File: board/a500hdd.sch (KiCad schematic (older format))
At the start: 35 parts, among them J1 Conn_01x04_Male, U1 ata_connector, U2 ata_connector44, U3 74LS04, U4 a500exp, U5 74LS00, U6 74LS08, U7 74LS08, U8 a500exp, U9 a500exp

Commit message: fixed activity LED on schematic?
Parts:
- removed unit 1 of U5
- added R19, R20: 10k, Capacitor_SMD:C_0805_2012Metric, symbol Device:R
- added unit 6 of U3
- added unit 4 of U5
- R18: value 4k7 -> 10k
- U3: value 74LS04 -> 74HCT14; symbol 74xx:74LS04 -> 74xx:74LS14
- U5: value 74LS00 -> 74HCT00
- U6, U7: value 74LS08 -> 74HCT08
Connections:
- net labels added: ~ATA40_ACTILED, ~ATA44_ACTILED
- net labels removed: B11, B9, ~ATA_ACTILED
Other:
- moved on the sheet: C1, C2, C3, C4, D1, R17, U5E

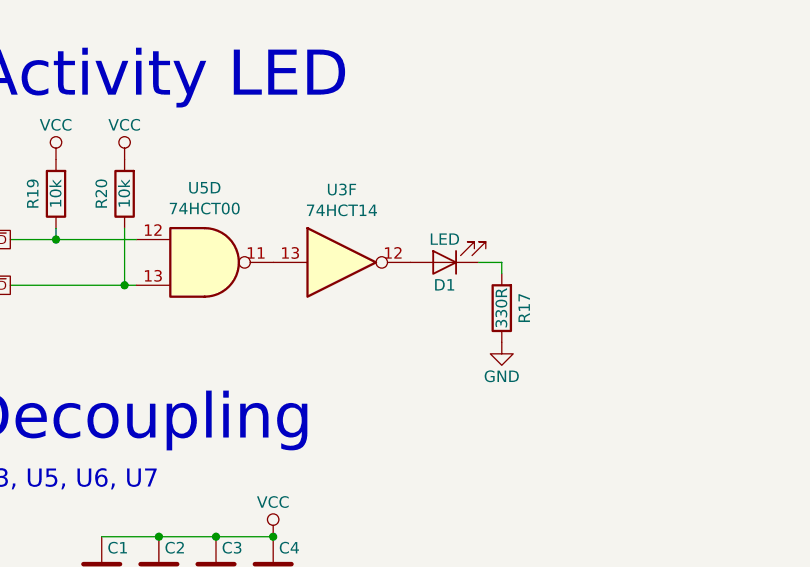
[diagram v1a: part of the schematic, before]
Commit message: Single negation of LED signal by NAND should be enough
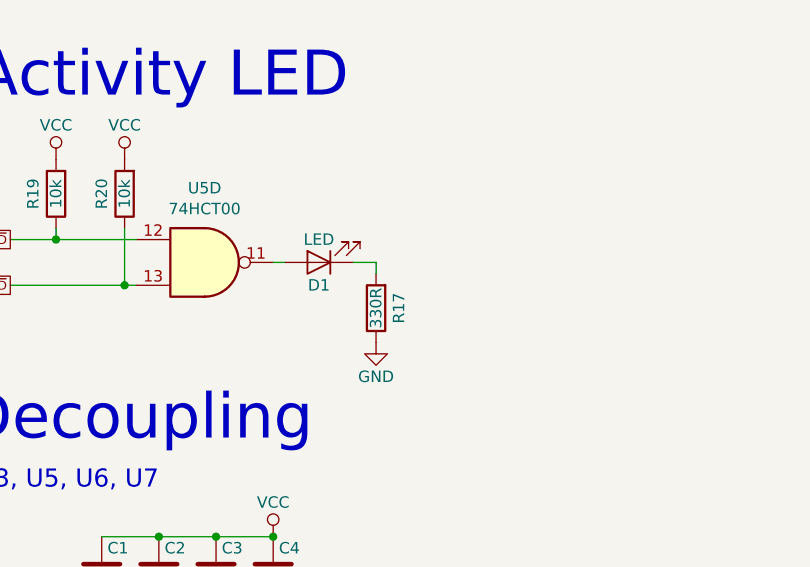
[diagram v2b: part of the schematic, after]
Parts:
- removed unit 6 of U3
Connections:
- wire segments 240 -> 241
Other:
- moved on the sheet: D1, R17
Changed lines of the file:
@@
 L Device:R R17
 U 1 1 59849A7F
-P 7900 5800
-F 0 "R17" V 7800 5800 50  0000 C CNN
-F 1 "330R" V 7900 5800 50  0000 C CNN
-F 2 "Capacitor_SMD:C_0805_2012Metric" V 7830 5800 50  0001 C CNN
-F 3 "" H 7900 5800 50  0000 C CNN
-	1    7900 5800
+P 7350 5800
+F 0 "R17" V 7250 5800 50  0000 C CNN
+F 1 "330R" V 7350 5800 50  0000 C CNN
+F 2 "Capacitor_SMD:C_0805_2012Metric" V 7280 5800 50  0001 C CNN
+F 3 "" H 7350 5800 50  0000 C CNN
+	1    7350 5800
 	-1   0    0    1
 $EndComp
@@
 L Device:LED D1
 U 1 1 59849BB3
-P 7650 5600
-F 0 "D1" H 7650 5700 50  0000 C CNN
-F 1 "LED" H 7650 5500 50  0000 C CNN
-F 2 "LED_SMD:LED_0805_2012Metric" H 7650 5600 50  0001 C CNN
-F 3 "" H 7650 5600 50  0000 C CNN
-	1    7650 5600
+P 7100 5600
+F 0 "D1" H 7100 5700 50  0000 C CNN
+F 1 "LED" H 7100 5500 50  0000 C CNN
+F 2 "LED_SMD:LED_0805_2012Metric" H 7100 5600 50  0001 C CNN
+F 3 "" H 7100 5600 50  0000 C CNN
+	1    7100 5600
 	-1   0    0    1
 $EndComp
 Wire Wire Line
-	7900 5600 7900 5650
+	7350 5600 7350 5650
 $Comp
 L power:GND #PWR09
 U 1 1 59849E9B
-P 7900 5950
-F 0 "#PWR09" H 7900 5700 50  0001 C CNN
-F 1 "GND" H 7900 5800 50  0000 C CNN
-F 2 "" H 7900 5950 50  0000 C CNN
-F 3 "" H 7900 5950 50  0000 C CNN
-	1    7900 5950
+P 7350 5950
+F 0 "#PWR09" H 7350 5700 50  0001 C CNN
+F 1 "GND" H 7350 5800 50  0000 C CNN
+F 2 "" H 7350 5950 50  0000 C CNN
+F 3 "" H 7350 5950 50  0000 C CNN
+	1    7350 5950
 	1    0    0    -1
 $EndComp
@@
 	950  3400 1050 3400
 Wire Wire Line
-	7800 5600 7900 5600
+	7250 5600 7350 5600
 Wire Wire Line
 	1450 10700 1550 10700
@@
 	1    0    0    -1
 $EndComp
-$Comp
-L 74xx:74LS14 U3
-U 6 1 5BB5917B
-P 7200 5600
-F 0 "U3" H 7200 5917 50  0000 C CNN
-F 1 "74HCT14" H 7200 5826 50  0000 C CNN
-F 2 "Package_SO:SOIC-14_3.9x8.7mm_P1.27mm" H 7200 5600 50  0001 C CNN
-F 3 "http://www.ti.com/lit/gpn/sn74LS04" H 7200 5600 50  0001 C CNN
-	6    7200 5600
-	1    0    0    -1
-$EndComp
 Wire Wire Line
 	5950 5500 6300 5500
+Wire Wire Line
+	6900 5600 6950 5600
 Wire Bus Line
 	5000 1450 5000 3100

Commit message: added clockport connectors
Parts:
- removed C1: 0.1uF, Capacitor_SMD:C_0805_2012Metric, symbol Device:C
- removed JP1, JP2: SolderJumper_2_Bridged, Jumper:SolderJumper-2_P1.3mm_Open_Pad1.0x1.5mm, symbol Jumper:SolderJumper_2_Bridged
- removed U3: 74HCT14, Package_SO:SOIC-14_3.9x8.7mm_P1.27mm, symbol 74xx:74LS14
- removed unit 2 of U5
- removed unit 3 of U5
- removed U6, U7: 74HCT08, Package_SO:SOIC-14_3.9x8.7mm_P1.27mm, symbol 74xx:74LS08
- added C3, C5, C6, C7, C8: 0.1uF, Capacitor_SMD:C_0805_2012Metric, symbol Device:C
- added D1, D3: LED, LED_SMD:LED_0805_2012Metric, symbol Device:LED
- added J1: Conn_02x03_Odd_Even, symbol Connector_Generic:Conn_02x03_Odd_Even
- added JP1: Jumper_NO_Small, symbol Jumper:SolderJumper_2_Open
- added JP2, JP3, JP4, JP5: SolderJumper_3_Open, symbol Jumper:SolderJumper_3_Open
- added R17, R18, R19: 10k, Capacitor_SMD:C_0805_2012Metric, symbol Device:R
- added R20, R23: 330R, Capacitor_SMD:C_0805_2012Metric, symbol Device:R
- added U1, U7: 74LS688, symbol 74xx:74LS688
- added U10, U12: clockport_connector, symbol a500hdd:clockport_connector
- added unit 1 of U3
- added unit 3 of U3
- added unit 4 of U3
- added U4: 74LS139, symbol 74xx:74LS139
- added U5, U6, U8, U9: 74HC245, symbol 74xx:74HC245
- renumbered C2 to C1, C3 to C2, D1 to D2, J1 to J2, R19 to R21, R20 to R22, R17 to R24, R18 to R25, U1 to U11, U2 to U13, U8 to U14, U9 to U15, U4 to U2, U5 to U3
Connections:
- net labels added: A12, A13, A14, A15, A2, A3, A4, A5, ADDR, ATA_ACTI, ATA_EN, CP_ACTI, CP_CS0, CP_CS1, CP_CS2, CP_CS3, CP_EN, INT6, UADDR, UDATA, ~ATA_CS2, ~ATA_CS3, ~CP_CSA, ~CP_CSB, ~IOR, ~IOW, ~RESET
- net labels removed: ATA_A0, ATA_A1, ATA_A2, ENABLE, ~ATA_RD, ~ATA_RESET, ~ATA_WR
- wire segments 241 -> 468
- no-connect marks 54 -> 53
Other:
- note added: "Address buffering"
- note added: "Buffers"
- note added: "Clockport Enable"
- note added: "Clockport connectors"
- note added: "Data buffering"
- note added: "Decoders"
- note added: "Decoupling & power"
- note added: "IDE40 Power"
- note added: "IO Read/Write"
- note added: "LEDs"
- note added: "Unused"
- note added: "~CS~ demux"
- note added: "~CS~ selection"
- note removed: "(optional)"
- note removed: "ATA Read/Write"
- note removed: "Activity LED"
- note removed: "Decoupling"
- note removed: "IDE Power"
- note removed: "U3, U5, U6, U7"
- note removed: "~CS~ swap"
- moved on the sheet: C1, C2, D2, J2, R1, R10, R11, R12, R13, R14, R15, R16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

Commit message: assignments done
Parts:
- J1: footprint (none) -> Connector_PinHeader_2.54mm:PinHeader_2x03_P2.54mm_Vertical
- JP1: footprint (none) -> Connector_PinHeader_2.54mm:PinHeader_1x02_P2.54mm_Vertical
- JP2, JP3, JP4, JP5: footprint (none) -> Connector_PinHeader_2.54mm:PinHeader_1x03_P2.54mm_Vertical
- U1, U5, U6, U7, U8, U9: footprint (none) -> Package_SO:TSSOP-20_4.4x6.5mm_P0.65mm
- U10, U12: footprint (none) -> Connector_PinHeader_2.00mm:PinHeader_2x11_P2.00mm_Vertical
- U3: footprint Package_SO:SOIC-14_3.9x8.7mm_P1.27mm -> Package_SO:TSSOP-14_4.4x5mm_P0.65mm
- U4: footprint (none) -> Package_SO:TSSOP-16_4.4x5mm_P0.65mm
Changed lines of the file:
@@
 F 0 "U3" H 2450 7200 50  0000 L CNN
 F 1 "74HCT00" H 2550 6850 50  0000 L CNN
-F 2 "Package_SO:SOIC-14_3.9x8.7mm_P1.27mm" H 2700 6850 50  0001 C CNN
+F 2 "Package_SO:TSSOP-14_4.4x5mm_P0.65mm" H 2700 6850 50  0001 C CNN
 F 3 "http://www.ti.com/lit/gpn/sn74ls00" H 2700 6850 50  0001 C CNN
 	5    2700 6850
@@
 F 0 "U3" H 6800 9475 50  0000 C CNN
 F 1 "74HCT00" H 6800 9384 50  0000 C CNN
-F 2 "Package_SO:SOIC-14_3.9x8.7mm_P1.27mm" H 6800 9150 50  0001 C CNN
+F 2 "Package_SO:TSSOP-14_4.4x5mm_P0.65mm" H 6800 9150 50  0001 C CNN
 F 3 "http://www.ti.com/lit/gpn/sn74ls00" H 6800 9150 50  0001 C CNN
 	2    6800 9150
@@
 F 0 "U1" H 1250 10750 50  0000 L CNN
 F 1 "74LS688" H 1650 8600 50  0000 L CNN
-F 2 "" H 1550 9700 50  0001 C CNN
+F 2 "Package_SO:TSSOP-20_4.4x6.5mm_P0.65mm" H 1550 9700 50  0001 C CNN
 F 3 "http://www.ti.com/lit/gpn/sn74LS688" H 1550 9700 50  0001 C CNN
 	1    1550 9700
@@
 F 0 "U7" H 3700 10750 50  0000 L CNN
 F 1 "74LS688" H 4100 8600 50  0000 L CNN
-F 2 "" H 4000 9700 50  0001 C CNN
+F 2 "Package_SO:TSSOP-20_4.4x6.5mm_P0.65mm" H 4000 9700 50  0001 C CNN
 F 3 "http://www.ti.com/lit/gpn/sn74LS688" H 4000 9700 50  0001 C CNN
 	1    4000 9700
@@
 F 0 "U4" H 14750 8917 50  0000 C CNN
 F 1 "74LS139" H 14750 8826 50  0000 C CNN
-F 2 "" H 14750 8550 50  0001 C CNN
+F 2 "Package_SO:TSSOP-16_4.4x5mm_P0.65mm" H 14750 8550 50  0001 C CNN
 F 3 "http://www.ti.com/lit/gpn/sn74LS139" H 14750 8550 50  0001 C CNN
 	1    14750 8550
@@
 F 0 "U4" H 14750 9667 50  0000 C CNN
 F 1 "74LS139" H 14750 9576 50  0000 C CNN
-F 2 "" H 14750 9300 50  0001 C CNN
+F 2 "Package_SO:TSSOP-16_4.4x5mm_P0.65mm" H 14750 9300 50  0001 C CNN
 F 3 "http://www.ti.com/lit/gpn/sn74LS139" H 14750 9300 50  0001 C CNN
 	2    14750 9300
@@
 F 0 "U4" H 3300 7200 50  0000 L CNN
 F 1 "74LS139" H 3400 6850 50  0000 L CNN
-F 2 "" H 3550 6850 50  0001 C CNN
+F 2 "Package_SO:TSSOP-16_4.4x5mm_P0.65mm" H 3550 6850 50  0001 C CNN
 F 3 "http://www.ti.com/lit/gpn/sn74LS139" H 3550 6850 50  0001 C CNN
 	3    3550 6850
@@
 F 0 "U3" H 8800 9725 50  0000 C CNN
 F 1 "74HCT00" H 8800 9634 50  0000 C CNN
-F 2 "Package_SO:SOIC-14_3.9x8.7mm_P1.27mm" H 8800 9400 50  0001 C CNN
+F 2 "Package_SO:TSSOP-14_4.4x5mm_P0.65mm" H 8800 9400 50  0001 C CNN
 F 3 "http://www.ti.com/lit/gpn/sn74ls00" H 8800 9400 50  0001 C CNN
 	1    8800 9400
@@
 F 0 "JP4" H 12850 8705 50  0000 C CNN
 F 1 "SolderJumper_3_Open" H 12850 8614 50  0000 C CNN
-F 2 "" H 12850 8500 50  0001 C CNN
+F 2 "Connector_PinHeader_2.54mm:PinHeader_1x03_P2.54mm_Vertical" H 12850 8500 50  0001 C CNN
 F 3 "~" H 12850 8500 50  0001 C CNN
 	1    12850 8500
@@
 F 0 "JP5" H 12850 9455 50  0000 C CNN
 F 1 "SolderJumper_3_Open" H 12850 9364 50  0000 C CNN
-F 2 "" H 12850 9250 50  0001 C CNN
+F 2 "Connector_PinHeader_2.54mm:PinHeader_1x03_P2.54mm_Vertical" H 12850 9250 50  0001 C CNN
 F 3 "~" H 12850 9250 50  0001 C CNN
 	1    12850 9250
@@
 F 0 "JP2" H 11550 8705 50  0000 C CNN
 F 1 "SolderJumper_3_Open" H 11550 8614 50  0000 C CNN
-F 2 "" H 11550 8500 50  0001 C CNN
+F 2 "Connector_PinHeader_2.54mm:PinHeader_1x03_P2.54mm_Vertical" H 11550 8500 50  0001 C CNN
 F 3 "~" H 11550 8500 50  0001 C CNN
 	1    11550 8500
@@
 F 0 "JP3" H 11550 9455 50  0000 C CNN
 F 1 "SolderJumper_3_Open" H 11550 9364 50  0000 C CNN
-F 2 "" H 11550 9250 50  0001 C CNN
+F 2 "Connector_PinHeader_2.54mm:PinHeader_1x03_P2.54mm_Vertical" H 11550 9250 50  0001 C CNN
 F 3 "~" H 11550 9250 50  0001 C CNN
 	1    11550 9250
@@
 F 0 "U10" H 7950 5700 50  0000 C CNN
 F 1 "clockport_connector" V 8300 5000 50  0000 C CNN
-F 2 "" H 8050 5450 50  0001 C CNN
+F 2 "Connector_PinHeader_2.00mm:PinHeader_2x11_P2.00mm_Vertical" H 8050 5450 50  0001 C CNN
 F 3 "" H 8050 5450 50  0001 C CNN
 	1    8300 5400
@@
 F 0 "U12" H 10300 5700 50  0000 C CNN
 F 1 "clockport_connector" V 10650 5000 50  0000 C CNN
-F 2 "" H 10400 5450 50  0001 C CNN
+F 2 "Connector_PinHeader_2.00mm:PinHeader_2x11_P2.00mm_Vertical" H 10400 5450 50  0001 C CNN
 F 3 "" H 10400 5450 50  0001 C CNN
 	1    10650 5400
@@
 F 0 "U3" H 6800 10075 50  0000 C CNN
 F 1 "74HCT00" H 6800 9984 50  0000 C CNN
-F 2 "Package_SO:SOIC-14_3.9x8.7mm_P1.27mm" H 6800 9750 50  0001 C CNN
+F 2 "Package_SO:TSSOP-14_4.4x5mm_P0.65mm" H 6800 9750 50  0001 C CNN
 F 3 "http://www.ti.com/lit/gpn/sn74ls00" H 6800 9750 50  0001 C CNN
 	3    6800 9750
@@
 F 0 "U3" H 11250 10825 50  0000 C CNN
 F 1 "74HCT00" H 11250 10734 50  0000 C CNN
-F 2 "Package_SO:SOIC-14_3.9x8.7mm_P1.27mm" H 11250 10500 50  0001 C CNN
+F 2 "Package_SO:TSSOP-14_4.4x5mm_P0.65mm" H 11250 10500 50  0001 C CNN
 F 3 "http://www.ti.com/lit/gpn/sn74ls00" H 11250 10500 50  0001 C CNN
 	4    11250 10500
@@
 F 0 "U6" H 3800 2600 50  0000 C CNN
 F 1 "74HC245" H 4200 1300 50  0000 C CNN
-F 2 "" H 4000 1950 50  0001 C CNN
+F 2 "Package_SO:TSSOP-20_4.4x6.5mm_P0.65mm" H 4000 1950 50  0001 C CNN
 F 3 "http://www.ti.com/lit/gpn/sn74HC245" H 4000 1950 50  0001 C CNN
 	1    4000 1950
@@
 F 0 "U9" H 5750 2600 50  0000 C CNN
 F 1 "74HC245" H 6150 1300 50  0000 C CNN
-F 2 "" H 5950 1950 50  0001 C CNN
+F 2 "Package_SO:TSSOP-20_4.4x6.5mm_P0.65mm" H 5950 1950 50  0001 C CNN
 F 3 "http://www.ti.com/lit/gpn/sn74HC245" H 5950 1950 50  0001 C CNN
 	1    5950 1950
@@
 F 0 "U5" H 4150 5050 50  0000 C CNN
 F 1 "74HC245" H 3750 3750 50  0000 C CNN
-F 2 "" H 3950 4400 50  0001 C CNN
+F 2 "Package_SO:TSSOP-20_4.4x6.5mm_P0.65mm" H 3950 4400 50  0001 C CNN
 F 3 "http://www.ti.com/lit/gpn/sn74HC245" H 3950 4400 50  0001 C CNN
 	1    3950 4400
@@
 F 0 "U8" H 6000 5050 50  0000 C CNN
 F 1 "74HC245" H 5600 3750 50  0000 C CNN
-F 2 "" H 5800 4400 50  0001 C CNN
+F 2 "Package_SO:TSSOP-20_4.4x6.5mm_P0.65mm" H 5800 4400 50  0001 C CNN
 F 3 "http://www.ti.com/lit/gpn/sn74HC245" H 5800 4400 50  0001 C CNN
 	1    5800 4400
@@
 F 0 "JP1" H 2950 9650 50  0000 C CNN
 F 1 "Jumper_NO_Small" V 2700 9550 50  0000 C CNN
-F 2 "" H 2950 9550 50  0001 C CNN
+F 2 "Connector_PinHeader_2.54mm:PinHeader_1x02_P2.54mm_Vertical" H 2950 9550 50  0001 C CNN
 F 3 "~" H 2950 9550 50  0001 C CNN
 	1    2950 9550
@@
 F 0 "J1" H 7350 11067 50  0000 C CNN
 F 1 "Conn_02x03_Odd_Even" H 7350 10976 50  0000 C CNN
-F 2 "" H 7300 10750 50  0001 C CNN
+F 2 "Connector_PinHeader_2.54mm:PinHeader_2x03_P2.54mm_Vertical" H 7300 10750 50  0001 C CNN
 F 3 "~" H 7300 10750 50  0001 C CNN
 	1    7300 10750
@@
 	7700 10100 7700 9500
 Connection ~ 7550 10100
+$Comp
+L a500hdd:a500exp U15
+U 1 1 5B79FEE5
+P 14700 4000
+F 0 "U15" H 14700 3900 60  0000 C CNN
+F 1 "a500exp" H 14700 4100 60  0000 C CNN
+F 2 "a500hdd:A500_Expansion_slot" H 14500 3150 60  0001 C CNN
+F 3 "" H 14500 3150 60  0001 C CNN
+	1    14700 4000
+	1    0    0    -1
+$EndComp
 Wire Bus Line
 	14000 8250 14000 9200
@@
 Wire Bus Line
 	700  1000 700  3400
-$Comp
-L a500hdd:a500exp U15
-U 1 1 5B79FEE5
-P 14700 4000
-F 0 "U15" H 14700 3900 60  0000 C CNN
-F 1 "a500exp" H 14700 4100 60  0000 C CNN
-F 2 "a500hdd:A500_Expansion_slot" H 14500 3150 60  0001 C CNN
-F 3 "" H 14500 3150 60  0001 C CNN
-	1    14700 4000
-	1    0    0    -1
-$EndComp
 $EndSCHEMATC
